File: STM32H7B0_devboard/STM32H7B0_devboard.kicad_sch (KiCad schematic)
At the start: 85 parts, among them J1 SWD, J2 24LC512 socet, J4 PORT_A, J5 PORT_B, J6 PORT_C, J7 PORT_D, J8 PORT_E, J9 Power_Conn, Q1 S8050, U1 STM32H7B0VBT6, Y1 32.768KHz, Y2 25MHz

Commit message: Started on V2
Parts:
- removed C14: 100n, Capacitor_SMD:C_0402_1005Metric, symbol Device:C_Small
- removed D1: Red, Diode_SMD:D_0603_1608Metric, symbol Device:LED_Small
- removed D2: Blue, Diode_SMD:D_0603_1608Metric, symbol Device:LED_Small
- removed J1: SWD, Connector_PinSocket_2.00mm:PinSocket_2x05_P2.00mm_Vertical, symbol Connector_Generic:Conn_02x05_Odd_Even
- removed J2: 24LC512 socet, Package_DIP:CERDIP-8_W7.62mm_SideBrazed_Socket, symbol Connector_Generic:Conn_02x04_Counter_Clockwise
- removed J4: PORT_A, Connector_PinSocket_2.00mm:PinSocket_1x16_P2.00mm_Vertical, symbol Connector_Generic:Conn_01x16
- removed J5: PORT_B, Connector_PinSocket_2.00mm:PinSocket_1x16_P2.00mm_Vertical, symbol Connector_Generic:Conn_01x16
- removed J6: PORT_C, Connector_PinSocket_2.00mm:PinSocket_1x16_P2.00mm_Vertical, symbol Connector_Generic:Conn_01x16
- removed J7: PORT_D, Connector_PinSocket_2.00mm:PinSocket_1x16_P2.00mm_Vertical, symbol Connector_Generic:Conn_01x16
- removed J8: PORT_E, Connector_PinSocket_2.00mm:PinSocket_1x16_P2.00mm_Vertical, symbol Connector_Generic:Conn_01x16
- removed J9: Power_Conn, Connector_PinSocket_2.00mm:PinSocket_2x08_P2.00mm_Vertical, symbol Connector_Generic:Conn_02x08_Odd_Even
- removed JP1, JP10, JP11, JP12, JP13, JP14, JP15, JP16, JP17, JP18, JP19, JP2, JP20, JP21, JP22, JP3, JP4, JP5, JP6, JP7, JP8, JP9: ~, Jumper:SolderJumper-2_P1.3mm_Open_TrianglePad1.0x1.5mm, symbol Jumper:SolderJumper_2_Open
- removed Q1: S8050, Package_TO_SOT_SMD:SOT-23, symbol Transistor_BJT:S8050
- removed R1: 1k, Resistor_SMD:R_0603_1608Metric, symbol Device:R_Small
- removed R10, R11, R16, R9: 2k2, Resistor_SMD:R_0402_1005Metric, symbol Device:R_Small
- removed R12: 8r2, Resistor_SMD:R_0402_1005Metric, symbol Device:R_Small
- removed R13, R29: 10k, Resistor_SMD:R_0402_1005Metric, symbol Device:R_Small
- removed R17, R18, R8: 22, Resistor_SMD:R_0402_1005Metric, symbol Device:R_Small
- removed R23, R24, R25, R26, R27, R28: 0, Resistor_SMD:R_0603_1608Metric, symbol Device:R_Small
- removed U2: ~, Custom:FPC_30_soldered, symbol Marijn:1.9{dblquote} LCD_FPC_CONN
- removed U3: ~, Package_SO:PowerIntegrations_SO-8, symbol Marijn:M95P32
- removed Y1: 32.768KHz, Crystal:Crystal_SMD_3215-2Pin_3.2x1.5mm, symbol Device:Crystal
- removed Y2: 25MHz, Crystal:Crystal_SMD_3225-4Pin_3.2x2.5mm, symbol Device:Crystal_GND24
- added C18: 12p, Capacitor_SMD:C_0402_1005Metric, symbol Device:C_Small
- added D1: BAT54C, Package_TO_SOT_SMD:SOT-23, symbol Diode:BAT54C
- added D2: PWR, symbol Device:LED
- added D3: STATUS, symbol Device:LED
- added J2: JTAG, symbol Connector_Generic:Conn_01x04
- added J3: A, symbol Connector_Generic:Conn_01x15
- added SW1, SW2: BTN, symbol Switch:SW_Push
- added U2: ~, Custom:SOT-25, symbol Marijn:AP7343
- added U4: ~, symbol Marijn:M95P32
- added Y1: 25MHz, Crystal:Crystal_SMD_3225-4Pin_3.2x2.5mm, symbol Device:Crystal_GND24
- added Y2: 32.768 KHz, Crystal:Crystal_SMD_3215-2Pin_3.2x1.5mm, symbol Device:Crystal
- C1: value 4u7 -> 1u; footprint Capacitor_SMD:C_0402_1005Metric -> (none); LCSC C23733 -> (none)
- C10, C11: value 12p -> 2u2; LCSC C1547 -> C12530
- C12, C13: value 2u2 -> 100n; footprint Capacitor_SMD:C_0402_1005Metric -> (none); LCSC C12530 -> (none)
- C15: value 4u7 -> 12p; LCSC C23733 -> C1547
- C16: value 1u -> 12p; LCSC C52923 -> C1547
- C17: value 10n -> 12p; LCSC C15195 -> C1547
- C2: value 100n -> 1u; footprint Capacitor_SMD:C_0402_1005Metric -> (none); LCSC C1525 -> (none)
- C3, C4, C5, C6, C7: footprint Capacitor_SMD:C_0402_1005Metric -> (none); LCSC C1525 -> (none)
- C8: value 12p -> 4.7u; footprint Capacitor_SMD:C_0402_1005Metric -> (none); LCSC C1547 -> (none)
- C9: value 12p -> 100n; footprint Capacitor_SMD:C_0402_1005Metric -> (none); LCSC C1547 -> (none)
- H1, H2, H3, H4: value Mount -> MountingHole_Pad; footprint MountingHole:MountingHole_4.3mm_M4_Pad_Via -> (none)
- L1: value 39n -> 10u; footprint Inductor_SMD:L_0603_1608Metric -> (none); LCSC C74308 -> (none)
- R14: value 1k -> 47; LCSC C11702 -> C25118
- R15: value 2k2 -> 47; LCSC C25879 -> C25118
- R2, R3: value 47 -> 10; footprint Resistor_SMD:R_0402_1005Metric -> (none); LCSC C25118 -> (none)
- R4: value 1k5 -> 5k1; footprint Resistor_SMD:R_0603_1608Metric -> (none); LCSC C22843 -> (none)
- R5: value 22 -> 1k; footprint Resistor_SMD:R_0402_1005Metric -> (none); LCSC C25092 -> (none)
- R6, R7: value 22 -> 10k; footprint Resistor_SMD:R_0402_1005Metric -> (none); LCSC C25092 -> (none)
- U1: value STM32H7B0VBT6 -> STM32H7B0VBTx; LCSC C730227 -> (none)
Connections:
- net J1_SWCLK is gone; now on net BOOT0: R6.1
- net J1_SWDIO is gone; now on net +3V3: R5.1
- net J1_SWO is gone; now on net +3V3: R7.1
- net +3.3VA: now also C9.1, L1.2, U1.20 (VREF+); no longer C16.1, C17.1, L1.1
- net +3V3: now also C8.1, L1.1, R4.1, D1.2, J2.1 (Pin_1), SW1.2, U2.5 (VOUT), U4.8 (VCC); no longer C1.1, C15.1, L1.2, R15.2, U1.6 (VBAT)
- net +5V: now also C1.1, U2.1 (VIN), U2.3 (EN)
- net BOOT0: now also SW1.1
- net GND: now also C12.1, C13.1, R6.2, C18.2, D2.1 (K), J2.4 (Pin_4), SW2.2, U2.2 (GND), U4.4 (VSS), Y1.2, Y1.4; no longer C12.2, C13.2, R4.1
- net HSE_IN: now also C15.1, Y1.1; no longer C10.1, U1.12 (PH0)
- net HSE_OUT: now also R14.1; no longer R3.1, U1.13 (PH1)
- net LSE_IN: now also C17.1, Y2.1; no longer C8.1, U1.8 (PC14)
- net LSE_OUT: now also R15.1; no longer R2.1, U1.9 (PC15)
- net NRST: now also C13.2, R7.2, SW2.1
- net SWCLK: now also J2.3 (Pin_3); no longer R6.2
- net SWDIO: now also J2.2 (Pin_2); no longer R5.2
- net USB_DN: now also R3.1
- net USB_DP: now also R2.1
- net USB/USB_DP: now reaches R2.2
- net USB/USB_DP: no longer C9.1
- net at R14.2: now also C16.1, Y1.3
- net at C11.1: now also U1.73 (VCAP); no longer R3.2
- net at U1.48 (VCAP): now also C10.1; no longer C12.1
- net at R4.2: now also D2.2 (A)
- net A0: no longer names the net of U1.22 (PA0)
- net A1: no longer names the net of U1.23 (PA1)
- net A10: no longer names the net of U1.69 (PA10)
- net A15: no longer names the net of U1.77 (PA15)
- net A2: no longer names the net of U1.24 (PA2)
- net A3: no longer names the net of U1.25 (PA3)
- net A4: no longer names the net of U1.28 (PA4)
- net A5: no longer names the net of U1.29 (PA5)
- net A8: no longer names the net of U1.67 (PA8)
- net A9: no longer names the net of U1.68 (PA9)
- net B4: no longer names the net of U1.90 (PB4)
- net B5: no longer names the net of U1.91 (PB5)
- net B8: no longer names the net of U1.95 (PB8)
- net B9: no longer names the net of U1.96 (PB9)
- net C1 renamed STATUS
- net STATUS: now also D3.1 (K)
- net C10: no longer names the net of U1.78 (PC10)
- net C11: no longer names the net of U1.79 (PC11)
- net C12: no longer names the net of U1.80 (PC12)
- net C13: no longer names the net of U1.7 (PC13)
- net C2_C: no longer names the net of U1.17 (PC2_C)
- net C3_C: no longer names the net of U1.18 (PC3_C)
- net C4: no longer names the net of U1.32 (PC4)
- net C5: no longer names the net of U1.33 (PC5)
- net C6: no longer names the net of U1.63 (PC6)
- net C7: no longer names the net of U1.64 (PC7)
- net C8: no longer names the net of U1.65 (PC8)
- net C9: no longer names the net of U1.66 (PC9)
- net D0: no longer names the net of U1.81 (PD0)
- net D1: no longer names the net of U1.82 (PD1)
- net D10: no longer names the net of U1.57 (PD10)
- net D11: no longer names the net of U1.58 (PD11)
- net D12: no longer names the net of U1.59 (PD12)
- net D13: no longer names the net of U1.60 (PD13)
- net D14: no longer names the net of U1.61 (PD14)
- net D15: no longer names the net of U1.62 (PD15)
- net D2: no longer names the net of U1.83 (PD2)
- net D3: no longer names the net of U1.84 (PD3)
- net D4: no longer names the net of U1.85 (PD4)
- net D5: no longer names the net of U1.86 (PD5)
- net D6: no longer names the net of U1.87 (PD6)
- net D7: no longer names the net of U1.88 (PD7)
- net D8: no longer names the net of U1.55 (PD8)
- net D9: no longer names the net of U1.56 (PD9)
- net E0: no longer names the net of U1.97 (PE0)
- net E1: no longer names the net of U1.98 (PE1)
- net E10: no longer names the net of U1.40 (PE10)
- net E12: no longer names the net of U1.42 (PE12)
- net E13: no longer names the net of U1.43 (PE13)
- net E14: no longer names the net of U1.44 (PE14)
- net E15: no longer names the net of U1.45 (PE15)
- net E2: no longer names the net of U1.1 (PE2)
- net E3: no longer names the net of U1.2 (PE3)
- net E4: no longer names the net of U1.3 (PE4)
- net E5: no longer names the net of U1.4 (PE5)
- net E6: no longer names the net of U1.5 (PE6)
- net E7: no longer names the net of U1.37 (PE7)
- net E8: no longer names the net of U1.38 (PE8)
- net E9: no longer names the net of U1.39 (PE9)
- net I2C_SCL: no longer names the net of U1.92 (PB6)
- net I2C_SDA: no longer names the net of U1.93 (PB7)
- net LCD_BACKLIGHT: no longer names the net of U1.46 (PB10)
- net LCD_BACKLIGHT: no longer R14.1
- net LCD_COMMAND: no longer names the net of U1.53 (PB14)
- net LCD_RESET: no longer names the net of U1.47 (PB11)
- net QSPI1_IO0: no longer names the net of U1.35 (PB1)
- net QSPI1_IO1: no longer names the net of U1.34 (PB0)
- net QSPI1_IO2: no longer names the net of U1.31 (PA7)
- net QSPI1_IO3: no longer names the net of U1.30 (PA6)
- net QSPI1_NSS: no longer names the net of U1.41 (PE11)
- net QSPI1_SCK: no longer names the net of U1.36 (PB2)
- net SPI2_MOSI: no longer names the net of U1.54 (PB15)
- net SPI2_NSS: no longer names the net of U1.51 (PB12)
- net SPI2_NSS: no longer R15.1
- net SPI2_SCK: no longer names the net of U1.52 (PB13)
- net STATUS_LED: no longer names the net of U1.15 (PC0)
- net SWO: no longer names the net of U1.89 (PB3)
- net SWO: no longer R7.2
- new net: C18.1, R15.2, Y2.2
- new net: D3.2 (A), R5.2
- new net QSPI_CLK: U4.6 (CLK)
- new net QSPI_IO0: U4.5 (D-DQ0)
- new net QSPI_IO1: U4.2 (Q-DQ1)
- new net QSPI_IO2: U4.3 (NW-DQ2)
- new net QSPI_IO3: U4.7 (NH_DQ3)
- new net QSPI_NCS: U4.1 (NCS)
- new net USB/USB_DN: R3.2
- new net VBAT: C12.2, D1.3, U1.6 (VBAT)
- new net VB_IN: D1.1
- no-connect marks 10 -> 0
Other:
- removed sheet power
- added sheet LCD (lcd.kicad_sch)
- sheet USB: file USB.kicad_sch -> usb.kicad_sch
- sheet USB ports: added none; removed VBUS
- note added: "BOOT0 / NRST"
- note added: "Bypass / Filter"
- note added: "Crystal"
- note added: "JTAG"
- note added: "LED"
- note added: "Power"
- note added: "QSPI Flash"
- note added: "STM32H7B0VBT6"
- note added: "TODO: W25Q64? from current devboard!!"
- note added: "USB"
- note added: "VBAT"
- note removed: "3V3 Analog"
- note removed: "Added zero-ohm bridges because QSPI code is still in testing"
- note removed: "BOOT0"
- note removed: "Cload (per cap) = 2 * (Yload - Cstray) (Cstray = 2 ~ 10)"
- note removed: "I2C"
- note removed: "LSE / HSE"
- note removed: "M95P32"
- note removed: "STATUS LED"
- note removed: "STM32H7B0vbt6"
- note removed: "SWD"
- note removed: "TODO: - Add batery capability"
- note removed: "TODO: - cmd_pin needed/implemented this way? - NSS via SPI periph or GPIO?"
- note removed: "TODO: More filtering? (RNG uses analog)"
- note removed: "TODO: remove global labels ->"
- note removed: "USB/Power"
- company: Marijn Verschuren -> (none)
- title: STM32H7B0_devboard -> (none)

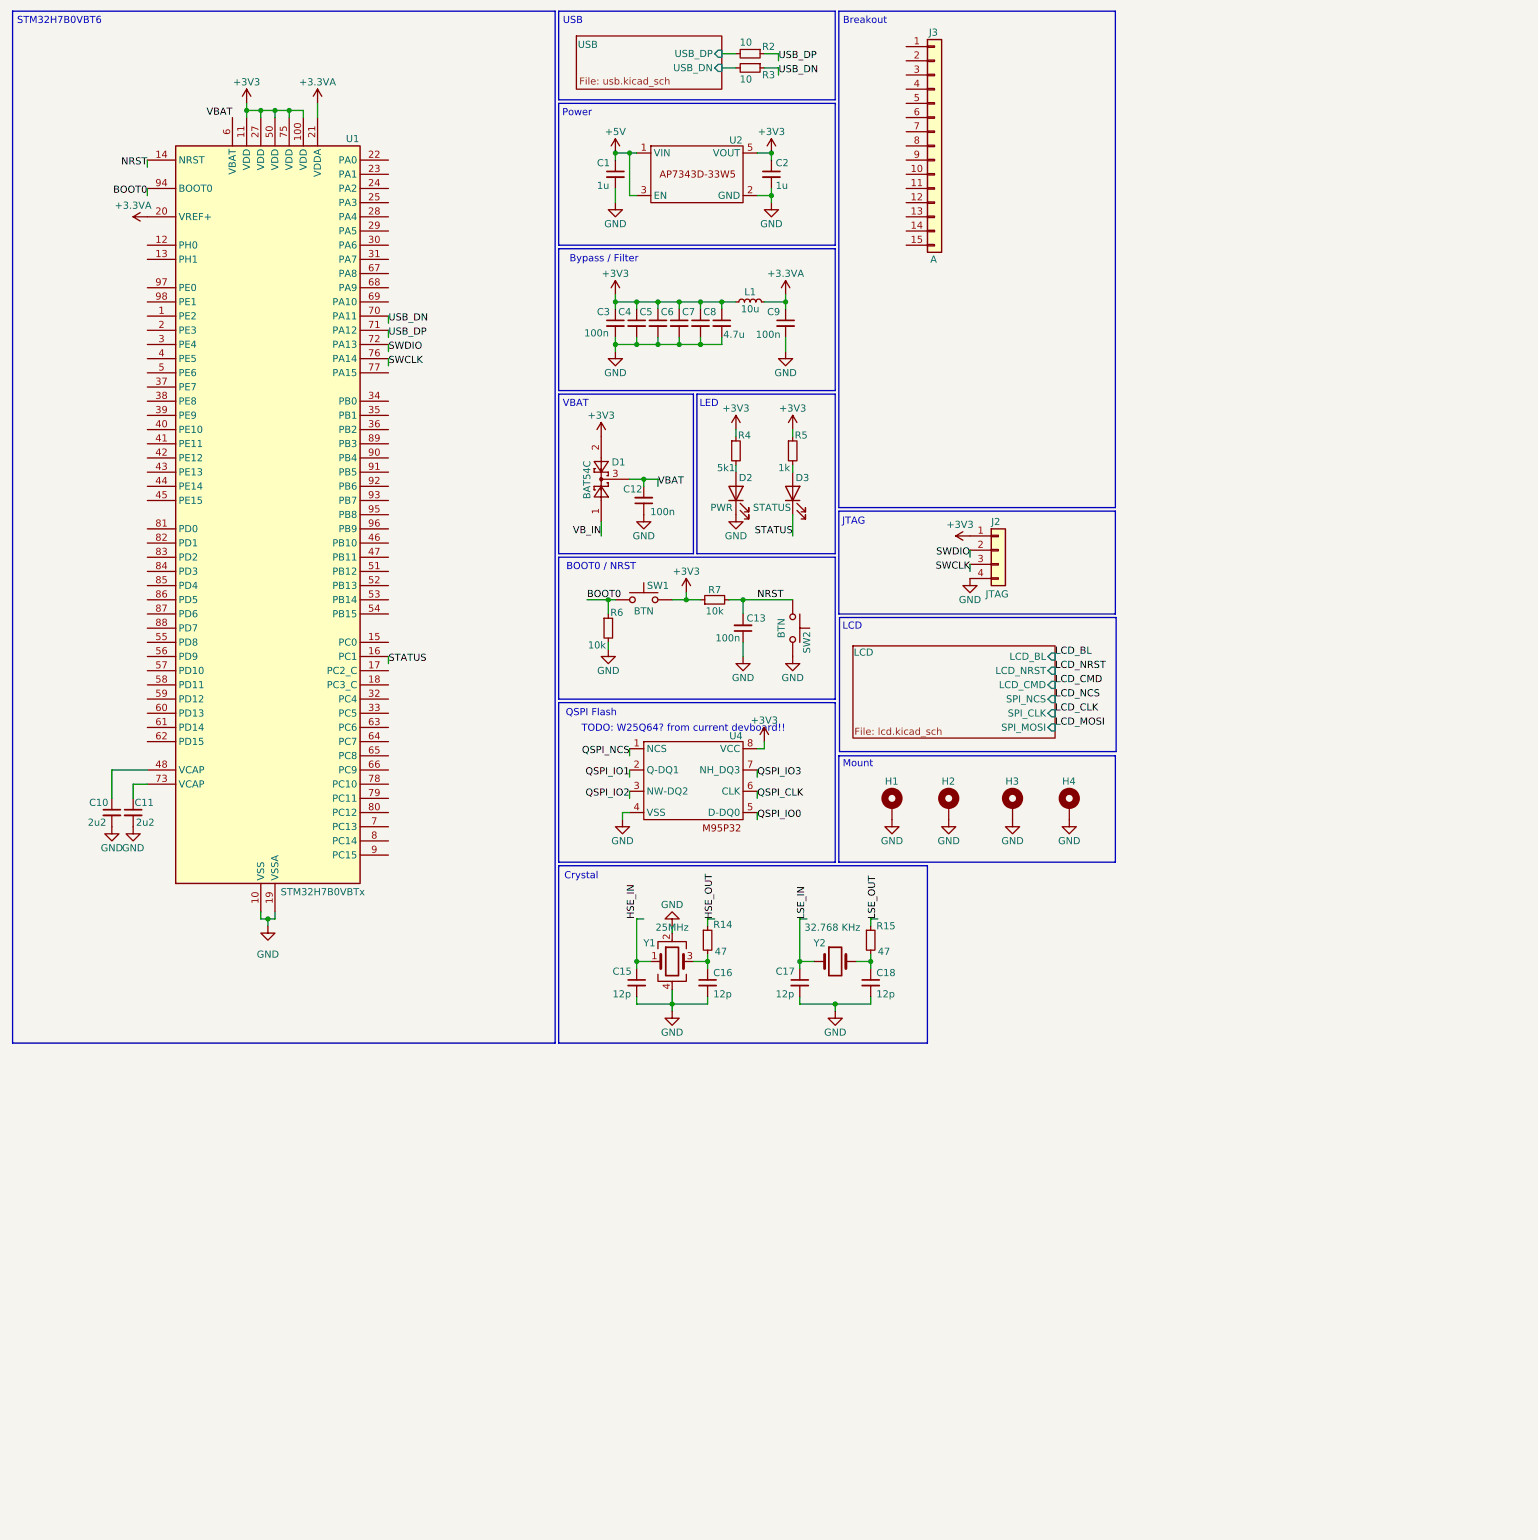
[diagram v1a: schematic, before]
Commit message: Upgraded QSPI flash
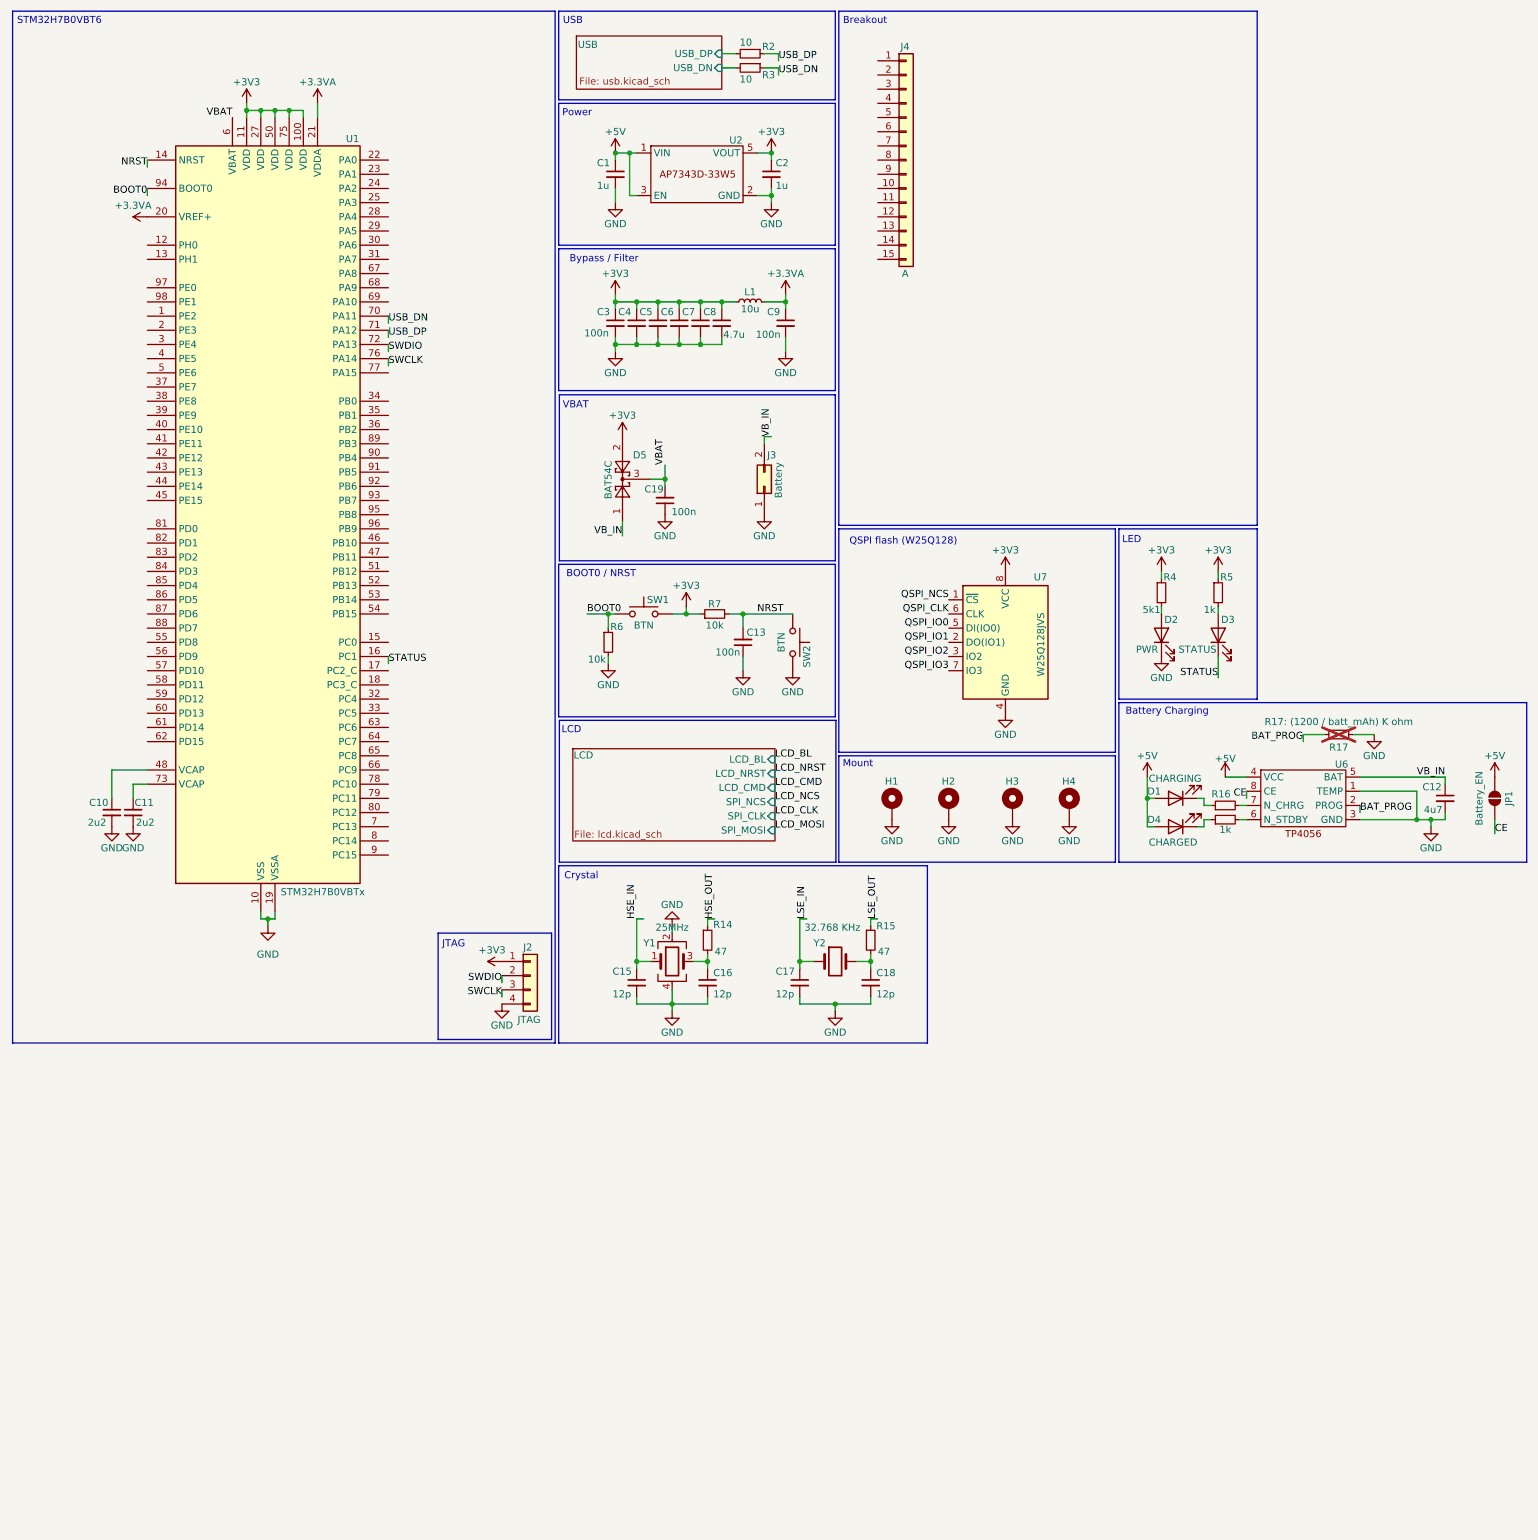
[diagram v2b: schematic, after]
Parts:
- removed D1: BAT54C, Package_TO_SOT_SMD:SOT-23, symbol Diode:BAT54C
- removed U4: ~, symbol Marijn:M95P32
- added C19: 100n, Capacitor_SMD:C_0603_1608Metric, symbol Device:C_Small
- added D1: CHARGING, LED_SMD:LED_0603_1608Metric, symbol Device:LED
- added D4: CHARGED, LED_SMD:LED_0603_1608Metric, symbol Device:LED
- added D5: BAT54C, Package_TO_SOT_SMD:SOT-23, symbol Diode:BAT54C
- added J3: Battery, Connector_PinHeader_2.00mm:PinHeader_1x02_P2.00mm_Vertical, symbol Connector_Generic:Conn_02x01
- added JP1: Battery_EN, Jumper:SolderJumper-2_P1.3mm_Open_TrianglePad1.0x1.5mm, symbol Jumper:SolderJumper_2_Open
- added R16, R18: 1k, Resistor_SMD:R_0603_1608Metric, symbol Device:R_Small
- added R17: R17: (1200 / batt_mAh) K ohm, Resistor_SMD:R_0603_1608Metric, symbol Device:R_Small
- added U6: ~, Package_SO:MSOP-8_3x3mm_P0.65mm, symbol Marijn:TP4056
- added U7: W25Q128JVS, Package_SO:SOIC-8_5.23x5.23mm_P1.27mm, symbol Memory_Flash:W25Q128JVS
- C12: value 100n -> 4u7; footprint (none) -> Capacitor_SMD:C_0603_1608Metric
- renumbered J3 to J4
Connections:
- net +3V3: now also D5.2, U7.8 (VCC)
- net +5V: now also D1.2 (A), D4.2 (A), JP1.1 (A), U6.4 (VCC)
- net GND: now also C12.2, C19.1, J3.1 (Pin_1), R17.2, U6.1 (TEMP), U6.3 (GND), U7.4 (GND); no longer C12.1
- net QSPI_CLK: now also U7.6 (CLK)
- net QSPI_IO0: now also U7.5 (DI(IO0))
- net QSPI_IO1: now also U7.2 (DO(IO1))
- net QSPI_IO2: now also U7.3 (IO2)
- net QSPI_IO3: now also U7.7 (IO3)
- net QSPI_NCS: now also U7.1 (~{CS})
- net VBAT: now also C19.2, D5.3; no longer C12.2
- net VB_IN: now also C12.1, D5.1, J3.2 (Pin_2), U6.5 (BAT)
- new net: D4.1 (K), R18.1
- new net: D1.1 (K), R16.1
- new net: R16.2, U6.7 (N_CHRG)
- new net: R18.2, U6.6 (N_STDBY)
- new net BAT_PROG: R17.1, U6.2 (PROG)
- new net CE: JP1.2 (B), U6.8 (CE)
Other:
- note added: "Battery Charging"
- note added: "QSPI flash (W25Q128)"
- note removed: "QSPI Flash"
- note removed: "TODO: W25Q64? from current devboard!!"
- moved on the sheet: C13, D2, D3, J2, J4, R4, R5, R6, R7, SW1, SW2
